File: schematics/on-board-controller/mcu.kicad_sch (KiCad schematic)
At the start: 8 parts, among them J2 programmer, U2 STM32L476RGTx

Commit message: updated on-board schematic with changes
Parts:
- added C13, C14: 100n, Capacitor_SMD:C_0805_2012Metric_Pad1.18x1.45mm_HandSolder, symbol Device:C
- R2: value 100k -> 10k
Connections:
- net +3V3: now also C13.2, C14.2
- net GND: now also C13.1, C14.1
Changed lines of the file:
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@@
+	)
+	(junction
+		(at 76.2 123.19)
+		(diameter 0)
+		(color 0 0 0 0)
 	)
 	(junction
@@
 	)
 	(junction
+		(at 88.9 111.76)
+		(diameter 0)
+		(color 0 0 0 0)
+	)
+	(junction
 		(at 48.26 44.45)
 		(diameter 0)
@@
 	)
 	(junction
+		(at 88.9 123.19)
+		(diameter 0)
+		(color 0 0 0 0)
+	)
+	(junction
 		(at 55.88 36.83)
 		(diameter 0)
@@
 		(color 0 0 0 0)
 	)
+	(junction
+		(at 76.2 111.76)
+		(diameter 0)
+		(color 0 0 0 0)
+	)
 	(no_connect
 		(at 127 82.55)
@@
 	(wire
 		(pts
+			(xy 104.14 123.19) (xy 88.9 123.19)
+		)
+		(stroke
+			(width 0)
+			(type default)
+		)
+	)
+	(wire
+		(pts
 			(xy 193.04 45.72) (xy 198.12 45.72)
 		)
@@
 	(wire
 		(pts
+			(xy 104.14 121.92) (xy 104.14 123.19)
+		)
+		(stroke
+			(width 0)
+			(type default)
+		)
+	)
+	(wire
+		(pts
 			(xy 118.11 46.99) (xy 127 46.99)
 		)
@@
 	(wire
 		(pts
+			(xy 88.9 111.76) (xy 88.9 114.3)
+		)
+		(stroke
+			(width 0)
+			(type default)
+		)
+	)
+	(wire
+		(pts
 			(xy 144.78 38.1) (xy 144.78 41.91)
 		)
@@
 	(wire
 		(pts
+			(xy 88.9 111.76) (xy 104.14 111.76)
+		)
+		(stroke
+			(width 0)
+			(type default)
+		)
+	)
+	(wire
+		(pts
 			(xy 162.56 49.53) (xy 198.12 49.53)
 		)
@@
 	(wire
 		(pts
+			(xy 76.2 123.19) (xy 88.9 123.19)
+		)
+		(stroke
+			(width 0)
+			(type default)
+		)
+	)
+	(wire
+		(pts
 			(xy 45.72 123.19) (xy 45.72 121.92)
 		)
@@
 	(wire
 		(pts
+			(xy 88.9 121.92) (xy 88.9 123.19)
+		)
+		(stroke
+			(width 0)
+			(type default)
+		)
+	)
+	(wire
+		(pts
 			(xy 189.23 53.34) (xy 198.12 53.34)
 		)
@@
 	(wire
 		(pts
+			(xy 76.2 111.76) (xy 88.9 111.76)
+		)
+		(stroke
+			(width 0)
+			(type default)
+		)
+	)
+	(wire
+		(pts
 			(xy 176.53 125.73) (xy 176.53 124.46)
 		)
@@
 		(pts
 			(xy 162.56 120.65) (xy 166.37 120.65)
+		)
+		(stroke
+			(width 0)
+			(type default)
+		)
+	)
+	(wire
+		(pts
+			(xy 104.14 111.76) (xy 104.14 114.3)
 		)
 		(stroke
@@
 			)
 		)
-		(property "Value" "100k"
+		(property "Value" "10k"
 			(at 119.38 59.6899 0)
 			(effects
@@
 	(symbol
 		(lib_id "Device:C")
+		(at 88.9 118.11 0)
+		(mirror x)
+		(unit 1)
+		(exclude_from_sim no)
+		(in_bom yes)
+		(on_board yes)
+		(dnp no)
+		(fields_autoplaced yes)
+		(property "Reference" "C13"
+			(at 92.71 119.3801 0)
+			(effects
+				(font
+					(size 1.27 1.27)
+				)
+				(justify left)
+			)
+		)
+		(property "Value" "100n"
+			(at 92.71 116.8401 0)
+			(effects
+				(font
+					(size 1.27 1.27)
+				)
+				(justify left)
+			)
+		)
+		(property "Footprint" "Capacitor_SMD:C_0805_2012Metric_Pad1.18x1.45mm_HandSolder"
+			(at 89.8652 114.3 0)
+			(effects
+				(font
+					(size 1.27 1.27)
+				)
+				(hide yes)
+			)
+		)
+		(property "Datasheet" "~"
+			(at 88.9 118.11 0)
+			(effects
+				(font
+					(size 1.27 1.27)
+				)
+				(hide yes)
+			)
+		)
+		(property "Description" "Unpolarized capacitor"
+			(at 88.9 118.11 0)
+			(effects
+				(font
+					(size 1.27 1.27)
+				)
+				(hide yes)
+			)
+		)
+		(pin "1"
+		)
+		(pin "2"
+		)
+		(instances
+			(project "sub"
+				(path "/aba2230e-80ca-41f8-a78f-a68ad044f9a5/5fbd2258-129b-4941-ab1b-b7cfedce7c9d"
+					(reference "C13")
+					(unit 1)
+				)
+			)
+		)
+	)
+	(symbol
+		(lib_id "Device:C")
 		(at 55.88 40.64 0)
 		(mirror x)
@@
 					(unit 1)
 				)
+			)
+		)
+	)
+	(symbol
+		(lib_id "Device:C")
+		(at 104.14 118.11 0)
+		(mirror x)
+		(unit 1)
+		(exclude_from_sim no)
+		(in_bom yes)
+		(on_board yes)
+		(dnp no)
+		(fields_autoplaced yes)
+		(property "Reference" "C14"
+			(at 107.95 119.3801 0)
+			(effects
+				(font
+					(size 1.27 1.27)
+				)
+				(justify left)
+			)
+		)
+		(property "Value" "100n"
+			(at 107.95 116.8401 0)
+			(effects
+				(font
+					(size 1.27 1.27)
+				)
+				(justify left)
+			)
+		)
+		(property "Footprint" "Capacitor_SMD:C_0805_2012Metric_Pad1.18x1.45mm_HandSolder"
+			(at 105.1052 114.3 0)
+			(effects
+				(font
+					(size 1.27 1.27)
+				)
+				(hide yes)
+			)
+		)
+		(property "Datasheet" "~"
+			(at 104.14 118.11 0)
+			(effects
+				(font
+					(size 1.27 1.27)
+				)
+				(hide yes)
+			)
+		)
+		(property "Description" "Unpolarized capacitor"
+			(at 104.14 118.11 0)
+			(effects
+				(font
+					(size 1.27 1.27)
+				)
+				(hide yes)
+			)
+		)
+		(pin "1"
+		)
+		(pin "2"
+		)
+		(instances
+			(project "sub"
+				(path "/aba2230e-80ca-41f8-a78f-a68ad044f9a5/5fbd2258-129b-4941-ab1b-b7cfedce7c9d"
+					(reference "C14")
+					(unit 1)
+				)

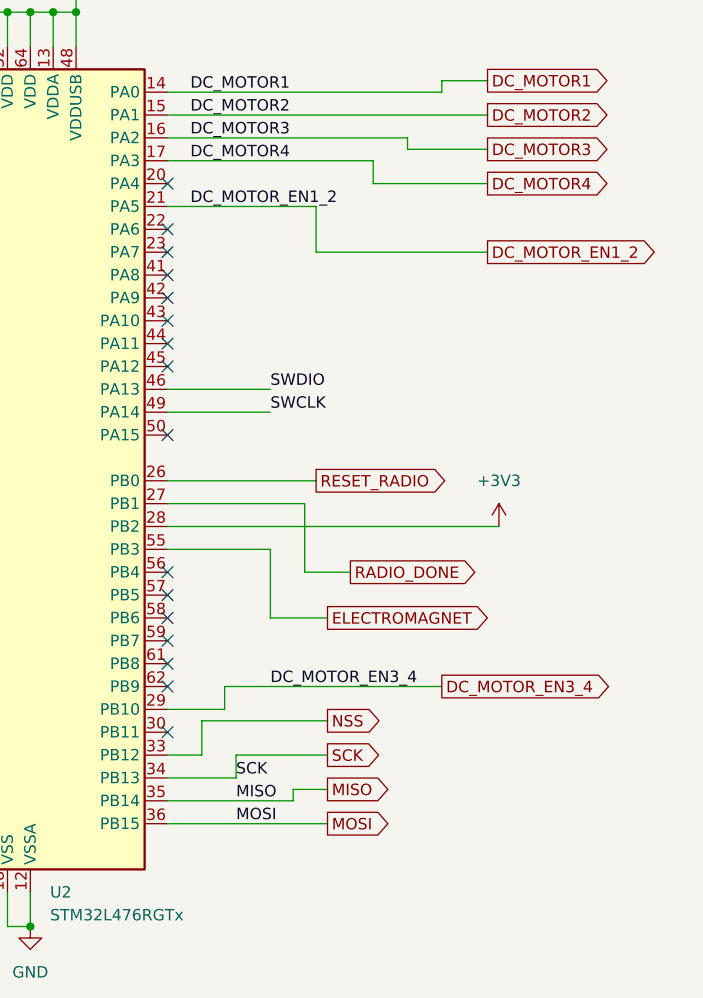
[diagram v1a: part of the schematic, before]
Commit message: on-board: updated schematic to match STM32 confighuration
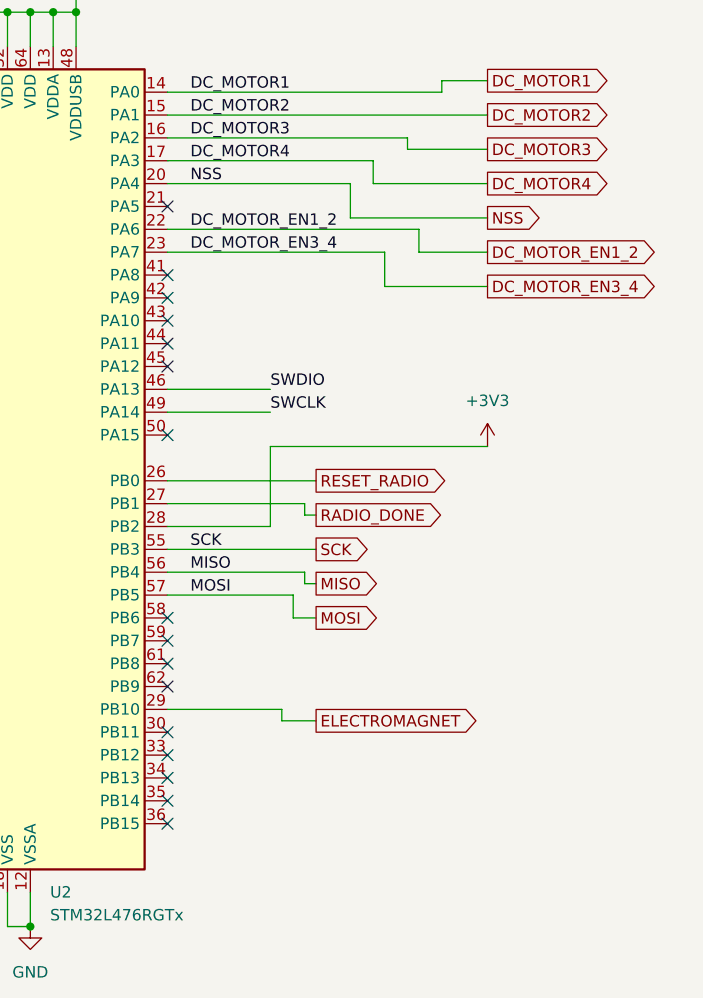
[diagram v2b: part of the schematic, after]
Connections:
- net DC_MOTOR_EN1_2: now also U2.22 (PA6); no longer U2.21 (PA5)
- net DC_MOTOR_EN3_4: now also U2.23 (PA7); no longer U2.29 (PB10)
- net ELECTROMAGNET: now also U2.29 (PB10); no longer U2.55 (PB3)
- net MISO: now also U2.56 (PB4); no longer U2.35 (PB14)
- net MOSI: now also U2.57 (PB5); no longer U2.36 (PB15)
- net NSS: now also U2.20 (PA4); no longer U2.33 (PB12)
- net SCK: now also U2.55 (PB3); no longer U2.34 (PB13)
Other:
- title: sumbersible -> On-board Controller

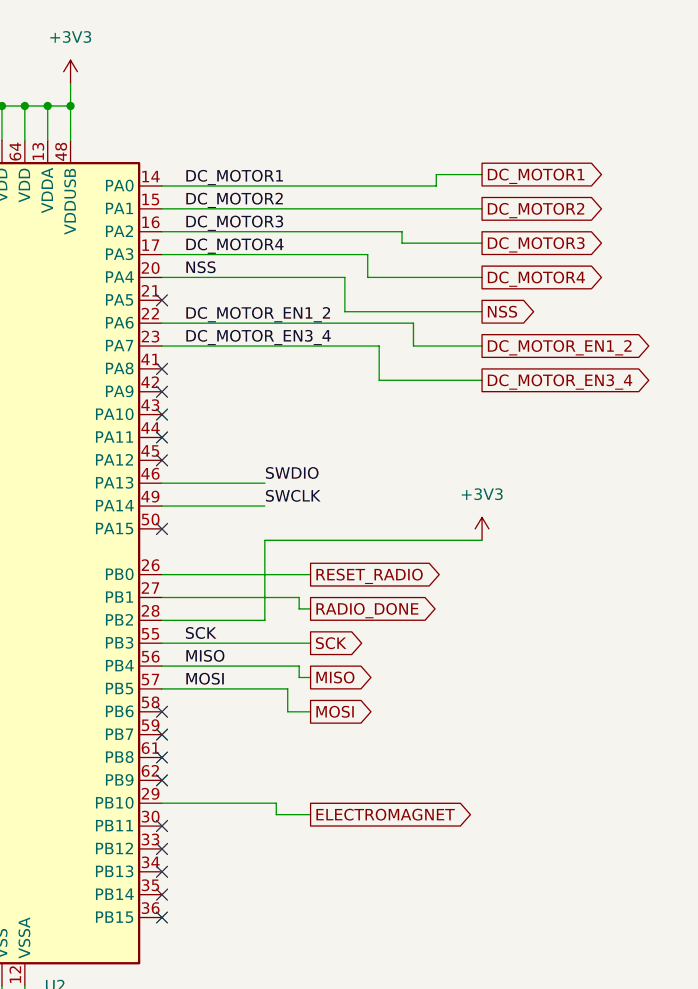
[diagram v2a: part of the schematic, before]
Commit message: off-board: created schematic
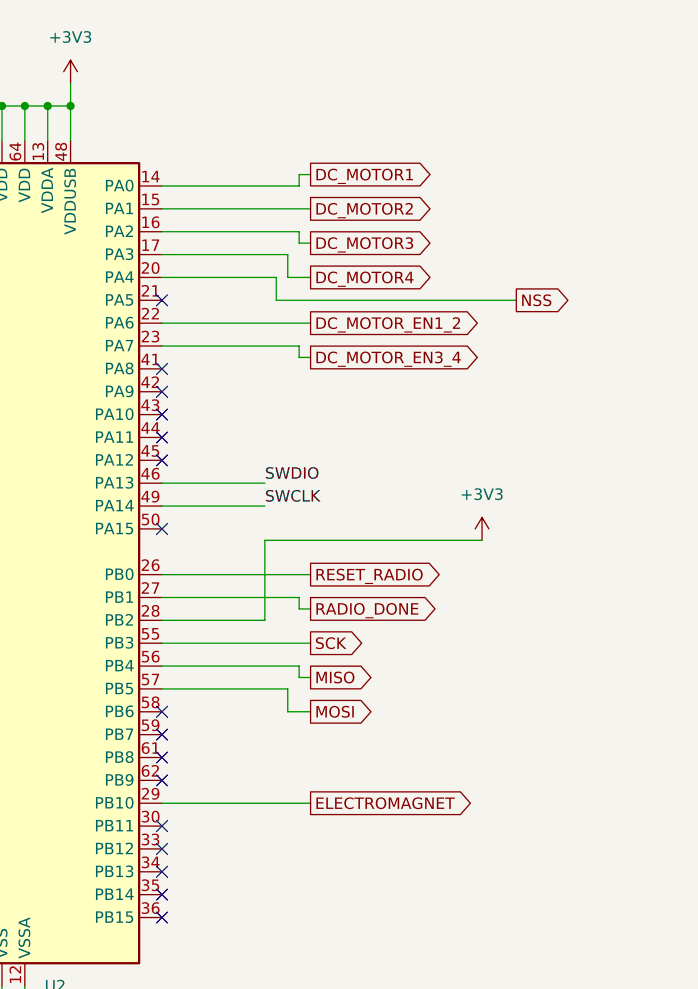
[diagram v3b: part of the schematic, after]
